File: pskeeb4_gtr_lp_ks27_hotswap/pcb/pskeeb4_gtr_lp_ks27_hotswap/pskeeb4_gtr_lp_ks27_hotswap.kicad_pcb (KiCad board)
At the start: 2 copper layers, 131.7 x 109.6 mm, 45 parts, among them K1 KEYSW, K10 KEYSW, K11 KEYSW, K12 KEYSW, K13 KEYSW, K14 KEYSW, K15 KEYSW, K16 KEYSW, K17 KEYSW, K18 KEYSW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

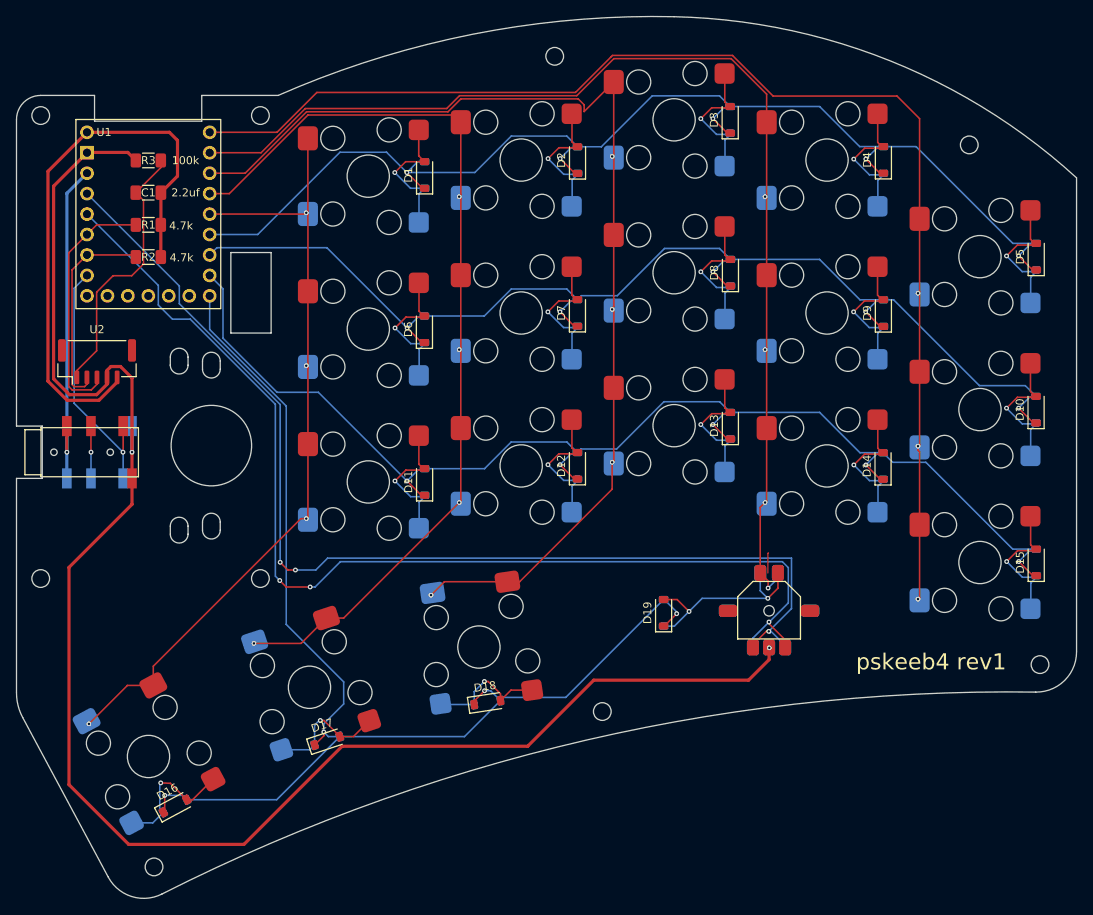
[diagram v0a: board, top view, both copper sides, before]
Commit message: feat: added hugebug trackball
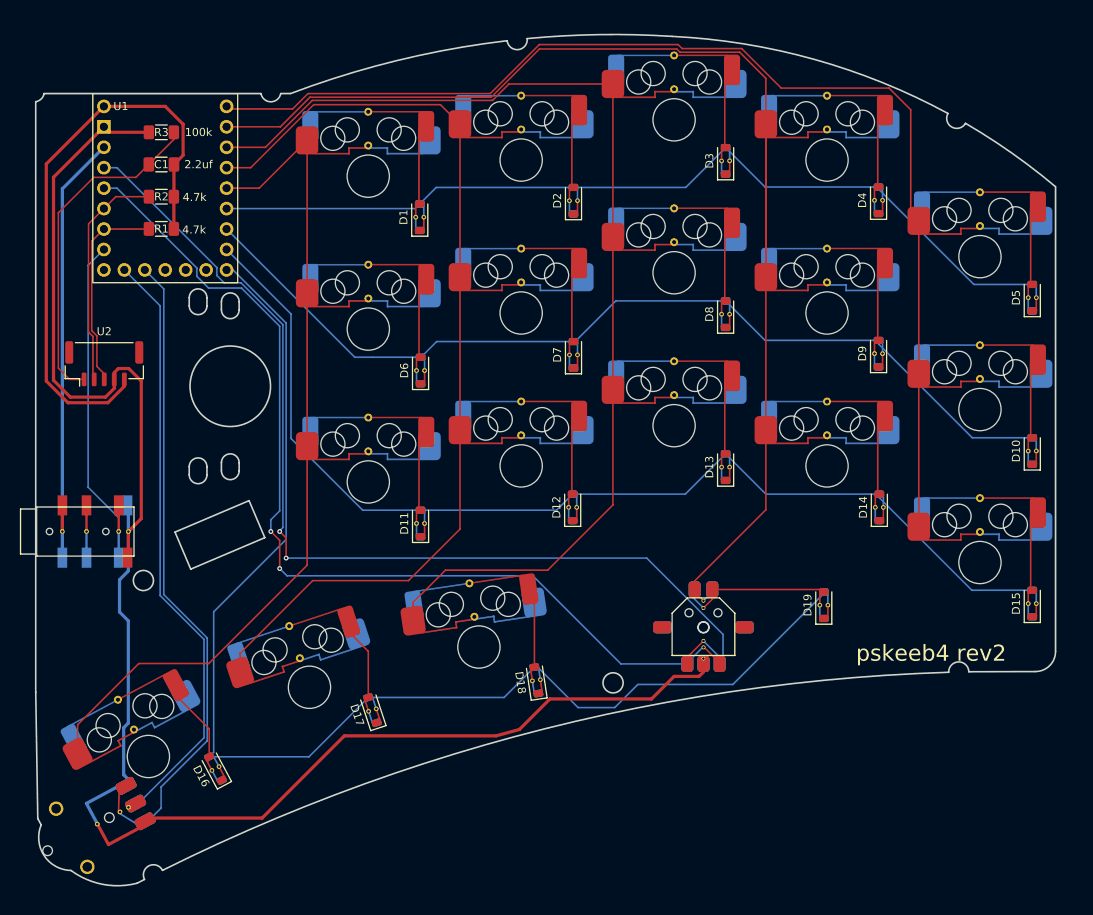
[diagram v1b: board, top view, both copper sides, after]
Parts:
- added SW2: RotaryEncoder, kwkb-footprint:nobole-rotary-encoder, F.Cu at (101.9, 134.2)
- moved D19 19.9 mm to (195.3, 105.2)
- moved U3 9.87 mm to (97.5, 96.1)
- moved SW1 8.40 mm to (180.3, 108.0)
- moved R2 7.67 mm to (113.0, 54.5)
- moved D16 6.85 mm to (119.7, 125.5), turned to 118.2 degrees
- moved D17 6.80 mm to (139.2, 118.3), turned to 108.304 degrees
- moved D18 6.69 mm to (159.6, 114.6), turned to 98.503 degrees
- moved D1 5.28 mm to (145.1, 57.0)
- moved D7 5.23 mm to (164.2, 74.2)
- moved D8 5.19 mm to (183.1, 69.1)
- moved D12 5.19 mm to (164.1, 93.1)
- moved D11 5.18 mm to (145.2, 95.1)
- moved D13 5.18 mm to (183.1, 88.1)
- moved D10 5.16 mm to (221.2, 86.1)
- moved D14 5.16 mm to (202.2, 93.1)
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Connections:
- R1 pad 2: PS2_CLK -> PS2_DAT
- R2 pad 2: PS2_DAT -> PS2_CLK
- U1 pad 10: unconnected-(U1-GP13-Pad10) -> ENA2
- U1 pad 11: unconnected-(U1-GP12-Pad11) -> ENB2
- U2 pad 2: PS2_DAT -> PS2_CLK
- U2 pad 3: PS2_CLK -> PS2_DAT
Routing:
- net ENB2: track 0.00 -> 74.2 mm
- net ENA2: track 0.00 -> 73.3 mm
- net row1: track 149.9 -> 110.4 mm, vias 5 -> 0
- net row2: track 146.0 -> 116.9 mm, vias 5 -> 0
- net GND: track 208.2 -> 184.0 mm, vias 2 -> 0
- net row3: track 155.6 -> 132.8 mm, vias 5 -> 0
- net ENB: track 137.9 -> 116.1 mm, vias 3 -> 2
- net col4: track 140.7 -> 158.7 mm, vias 4 -> 0
- net Net-(D19-A): track 28.4 -> 14.0 mm, vias 2 -> 0
- net ENA: track 137.0 -> 122.7 mm, vias 3 -> 2
- net col5: track 155.5 -> 144.0 mm, vias 3 -> 0
- net Net-(U2-RST): track 33.4 -> 42.1 mm
- net Net-(D4-A): track 17.6 -> 9.39 mm, vias 1 -> 0
- net Net-(D9-A): track 17.6 -> 9.44 mm, vias 1 -> 0
- net Net-(D2-A): track 17.6 -> 9.48 mm, vias 1 -> 0
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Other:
- board size 131.7 x 109.6 mm -> 126.7 x 105.8 mm
- board text added: "pskeeb4 rev2"
- board text removed: "pskeeb4 rev1"

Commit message: refactor: increase footprint pads for easier soldering
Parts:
- C1: footprint Capacitor_SMD:C_1206_3216Metric_Pad1.33x1.80mm_HandSolder -> kwkb-footprint:C_1206_3216Metric_Pad1.33x1.80mm_HandSolder
- R1, R2, R3: footprint Resistor_SMD:R_1206_3216Metric_Pad1.30x1.75mm_HandSolder -> kwkb-footprint:C_1206_3216Metric_Pad1.33x1.80mm_HandSolder
- U2: footprint Connector_JST:JST_GH_BM05B-GHS-TBT_1x05-1MP_P1.25mm_Vertical -> kwkb-footprint:JST_GH_BM05B-GHS-TBT_1x05-1MP_P1.25mm_Vertical
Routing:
- net +5V: track 73.8 -> 74.6 mm
